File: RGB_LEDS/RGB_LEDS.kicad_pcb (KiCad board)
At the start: 2 copper layers, 21.7 x 28.1 mm, 16 parts, among them IC1 ATTINY202-SSFR, IC2 INA180A4IDBVR, IC3 XC9140A501MR-G, J1 HCZZ0021-2, SW1 SW_Push, U1 MY-2032-08

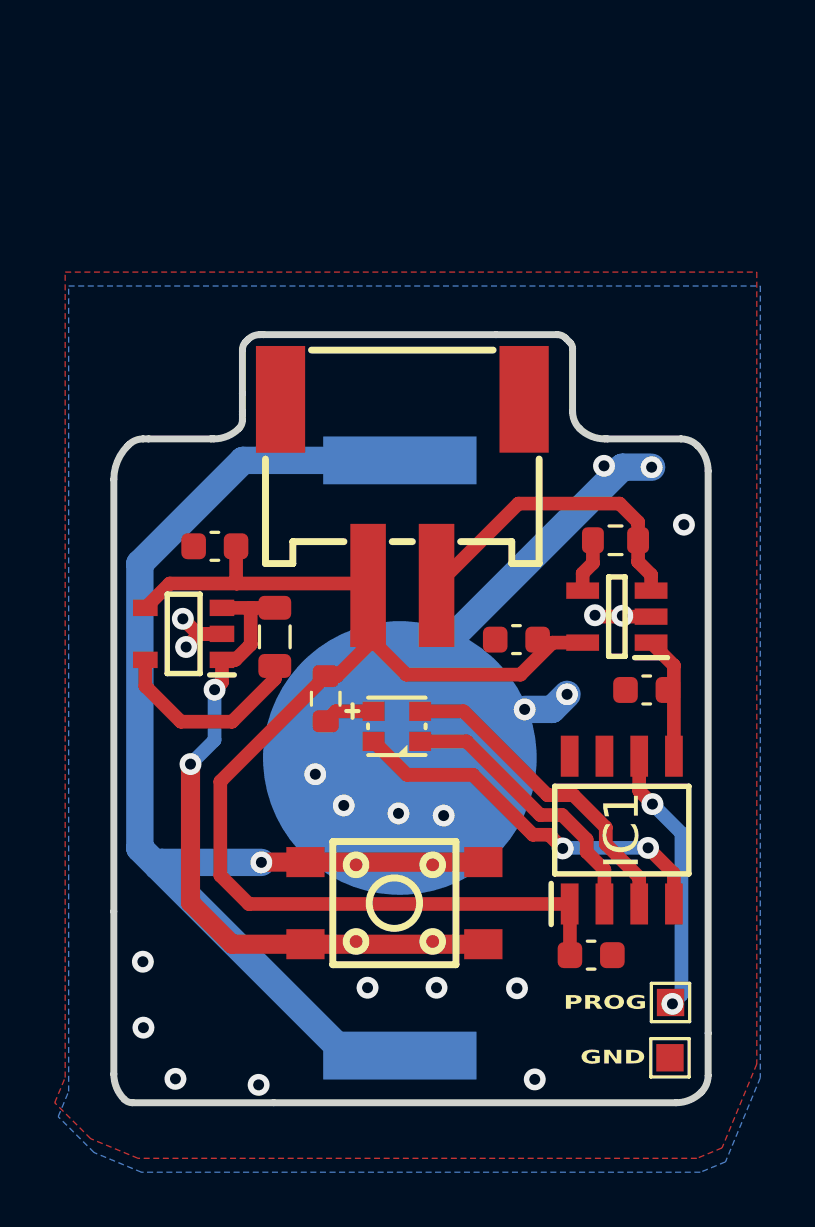
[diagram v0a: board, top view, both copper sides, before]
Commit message: Placa con stm32, selector de voltaje se necesita quitar una vez que se decida por un valor
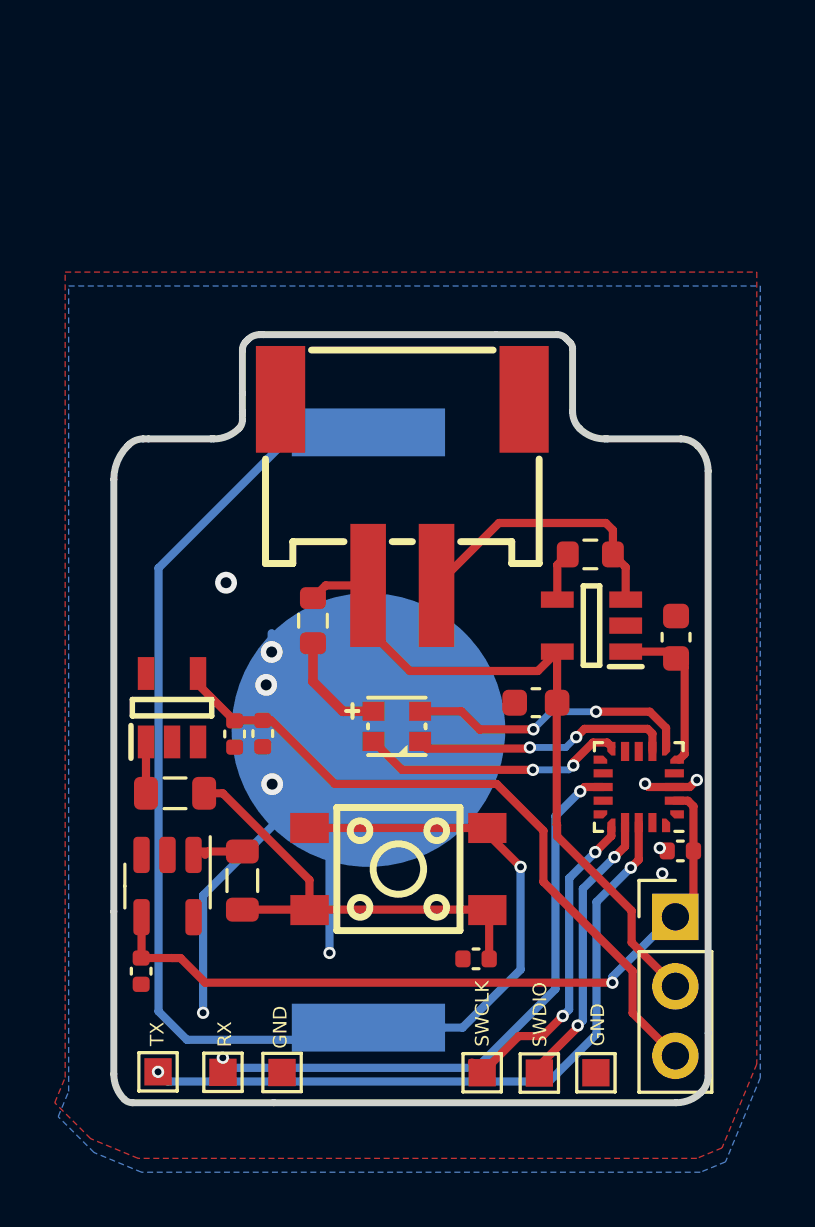
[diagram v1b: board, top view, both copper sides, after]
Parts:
- removed IC3: XC9140A501MR-G, SamacSys_Parts:SOT95P280X130-5N
- added C5: 100n, Capacitor_SMD:C_0402_1005Metric, F.Cu at (158.5, 99.8)
- added C6: 4.7u, Capacitor_SMD:C_0402_1005Metric, F.Cu at (165.9, 95.9)
- added C7: 100n, Capacitor_SMD:C_0402_1005Metric, F.Cu at (150.7, 91.6)
- added J2: Conn_01x03_Pin, Connector_PinHeader_2.54mm:PinHeader_1x03_P2.54mm_Vertical, F.Cu at (165.7, 98.3)
- added L2: 2.2u, Inductor_SMD:L_0805_2012Metric, F.Cu at (147.5, 93.8)
- added U3: STM32C011F4Ux, Package_DFN_QFN:ST_UFQFPN-20_3x3mm_P0.5mm, F.Cu at (164.4, 93.5)
- added U5: TPS613221ADBV, Package_TO_SOT_SMD:SOT-23-5, F.Cu at (147.2, 97.1)
- added U6: ~, TestPoint:TestPoint_Pad_1.0x1.0mm, F.Cu at (146.8, 103.9)
- added U7: ~, TestPoint:TestPoint_Pad_1.0x1.0mm, F.Cu at (160.8, 104.0)
- added U8: ~, TestPoint:TestPoint_Pad_1.0x1.0mm, F.Cu at (158.7, 104.0)
- added U9: ~, TestPoint:TestPoint_Pad_1.0x1.0mm, F.Cu at (162.8, 104.0)
- C2: footprint Capacitor_SMD:C_0603_1608Metric -> Capacitor_SMD:C_0402_1005Metric
- C4: value 100n -> 4.7u; footprint Capacitor_SMD:C_0603_1608Metric -> Capacitor_SMD:C_0402_1005Metric
- IC1: value ATTINY202-SSFR -> TPS613222ADBVR; footprint SamacSys_Parts:SOIC127P600X175-8N -> SamacSys_Parts:SOT95P280X145-5N
- L1: value 4.7u -> 2.2u
- moved IC1 17.0 mm to (147.4, 90.6)
- moved U4 16.3 mm to (149.2, 104.0), turned to 0 degrees
- moved C2 15.8 mm to (146.2, 100.3), turned to 90 degrees
- moved C4 15.3 mm to (149.6, 91.6), turned to -90 degrees
- moved U2 14.4 mm to (151.4, 104.0)
- moved L1 8.98 mm to (149.9, 96.9)
- moved R2 2.89 mm to (152.5, 87.4)
- moved C1 2.41 mm to (160.7, 90.4)
- moved C3 2.21 mm to (165.8, 88.1), turned to 90 degrees
- moved U1 1.54 mm to (154.5, 91.4)
- moved SW1 1.26 mm to (155.6, 96.5)
- moved R1 1.05 mm to (162.6, 85.0)
- moved IC2 0.98 mm to (162.7, 87.6)
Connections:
- C1 pad 1: +5V -> Vused
- C2 pad 2: +5V -> +3.3V
- IC1 pad 1: +5V -> Net-(IC1-SW)
- IC1 pad 2: R -> GND
- IC1 pad 3: G -> unconnected-(IC1-NC_1-Pad3)
- IC1 pad 4: B -> +5V
- IC1 pad 5: REF_OUT -> unconnected-(IC1-NC_2-Pad5)
- IC2 pad 5: +5V -> Vused
- J1 pad 1: +5V -> Vused
- L1 pad 1: Net-(IC3-LX) -> Net-(C5-Pad1)
- L1 pad 2: Net-(IC3-CE) -> Net-(U5-SW)
- R2 pad 2: +5V -> Vused
- SW1 pad 2: Net-(IC3-CE) -> Net-(C5-Pad1)
- U2 pad 1: Net-(IC1-PA0/~{RESET}/UPDI) -> GND
- U4 pad 1: GND -> RX
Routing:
- net +3.3V: track 0.00 -> 27.6 mm, vias 0 -> 1
- net Vused: track 0.00 -> 25.7 mm
- net TX: track 0.00 -> 25.3 mm, vias 0 -> 2
- net Net-(IC3-CE): track 25.2 -> 0.00 mm, vias 2 -> 0
- net +5V: track 48.8 -> 25.5 mm
- net RX: track 0.00 -> 22.0 mm, vias 0 -> 2
- net Net-(C5-Pad1): track 0.00 -> 17.0 mm
- net /SWCLK: track 0.00 -> 12.0 mm, vias 0 -> 2
- net /SWDIO: track 0.00 -> 10.5 mm, vias 0 -> 2
- net Net-(IC1-PA0/~{RESET}/UPDI): track 9.83 -> 0.00 mm, vias 2 -> 0
- net Net-(IC3-LX): track 7.35 -> 0.00 mm
- net Net-(SW1-Pad1): track 46.1 -> 53.2 mm
- net GND: track 26.1 -> 31.2 mm, vias 21 -> 10
- net B: track 14.1 -> 9.66 mm
- net Net-(D1-Pad3): track 1.90 -> 4.06 mm
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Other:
- board text added: "RX"
- board text added: "SWCLK"
- board text added: "SWDIO"
- board text added: "TX"
- board text removed: "PROG"

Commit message: final version, longer connector, 3.3 only
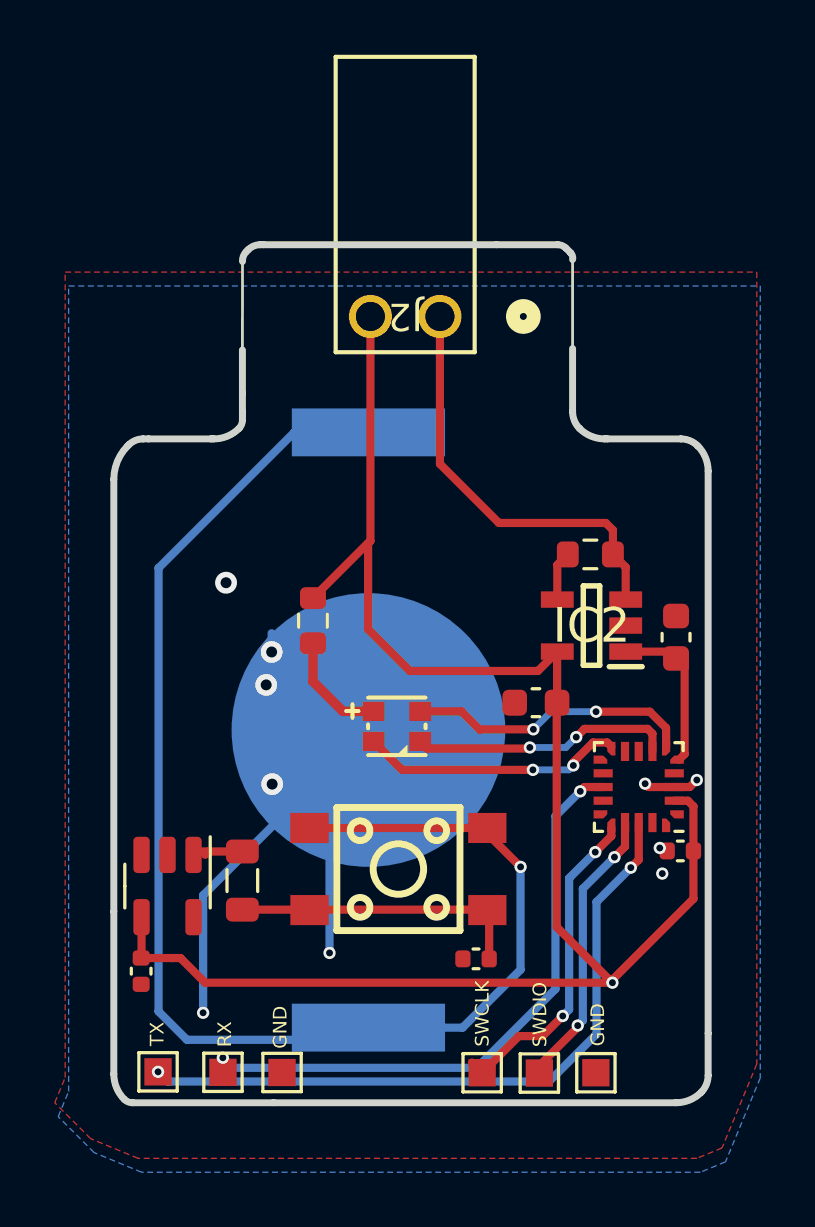
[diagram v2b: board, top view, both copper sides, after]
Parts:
- removed C4: 4.7u, Capacitor_SMD:C_0402_1005Metric
- removed C7: 100n, Capacitor_SMD:C_0402_1005Metric
- removed IC1: TPS613222ADBVR, SamacSys_Parts:SOT95P280X145-5N
- removed J1: HCZZ0021-2, Library:CONN-SMD_2P-P2.50-A2501-WF-02A
- removed L2: 2.2u, Inductor_SMD:L_0805_2012Metric
- IC2: footprint SamacSys_Parts:SOT95P280X145-5N -> SamacSys:SOT95P280X145-5N
- J2: value Conn_01x03_Pin -> 22122021; footprint Connector_PinHeader_2.54mm:PinHeader_1x03_P2.54mm_Vertical -> 0022122021:CONN_A-4094-02A_MOL
- U3: value STM32C011F4Ux -> STM32C011F6U6TR
- moved J2 23.6 mm to (157.1, 76.3), turned to 180 degrees
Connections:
- C1 pad 1: Vused -> +3.3V
- IC2 pad 5: Vused -> +3.3V
- J2 pad 1: +3.3V -> REF
- J2 pad 2: Vused -> +3.3V
- R2 pad 2: Vused -> +3.3V
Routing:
- net +3.3V: track 27.6 -> 62.6 mm
- net Vused: track 25.7 -> 0.00 mm
- net +5V: track 25.5 -> 0.00 mm
- net Net-(C5-Pad1): track 17.0 -> 10.8 mm
- net REF: track 10.2 -> 15.4 mm
- net Net-(IC1-SW): track 1.88 -> 0.00 mm
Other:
- board size 21.7 x 28.1 mm -> 21.7 x 31.4 mm

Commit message: Added selector
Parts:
- added S1: CL-SB-23B-01T, SamacSys_Parts:CLSB23B01T, F.Cu at (148.6, 87.5)
- SW1: value SW_Push -> TSC015A05026A
- moved R2 1.07 mm to (153.3, 88.1)
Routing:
- net Net-(D1-Pad3): track 4.06 -> 3.04 mm
- net GND: vias 10 -> 11
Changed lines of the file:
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@@
   (net 26 "unconnected-(U5-NC-Pad5)")
   (net 27 "Net-(SW1-Pad1)")
+  (net 28 "unconnected-(S1-NO_1-Pad1)")
+  (net 29 "unconnected-(S1-NC_1-Pad2)")
+  (net 30 "unconnected-(S1-COM_1-Pad3)")
+  (net 31 "unconnected-(S1-NO_2-Pad4)")
+  (net 32 "unconnected-(S1-NO_3-Pad5)")
+  (net 33 "unconnected-(S1-NC_2-Pad6)")
+  (net 34 "unconnected-(S1-COM_2-Pad7)")
+  (net 35 "unconnected-(S1-NO_4-Pad8)")
   (footprint "Resistor_SMD:R_0603_1608Metric" (layer "F.Cu")
     (at 162.641 85.027)
@@
         (effects (font (size 1.143 1.143) (thickness 0.1524)) (justify left))
     )
-    (fp_text value "SW_Push" (at 0 -5.116322) (layer "F.Fab") hide
+    (fp_text value "TSC015A05026A" (at 0 -5.116322) (layer "F.Fab") hide
         (effects (font (size 1.143 1.143) (thickness 0.1524)) (justify left))
     )
@@
   )
   (footprint "Resistor_SMD:R_0603_1608Metric" (layer "F.Cu")
-    (at 152.505 87.448 90)
+    (at 153.319 88.138 90)
     (descr "Resistor SMD 0603 (1608 Metric), square (rectangular) end terminal, IPC_7351 nominal, (Body size source: IPC-SM-782 page 72, https://www.pcb-3d.com/wordpress/wp-content/uploads/ipc-sm-782a_amendment_1_and_2.pdf), generated with kicad-footprint-generator")
     (tags "resistor")
@@
     (pad "1" smd rect (at 0 0) (size 1 1) (layers "F.Cu" "F.Mask")
       (net 21 "/SWDIO") (pinfunction "PAD") (pintype "input"))
+  )
+  (footprint "SamacSys_Parts:CLSB23B01T" (layer "F.Cu")
+    (at 148.634 87.451 90)
+    (descr "CL-SB-23B-01T-1")
+    (tags "Switch")
+    (property "Arrow Part Number" "")
+    (property "Arrow Price/Stock" "")
+    (property "Height" "3.5")
+    (property "Manufacturer_Name" "Nidec Copal")
+    (property "Manufacturer_Part_Number" "CL-SB-23B-01T")
+    (property "Mouser Part Number" "229-CL-SB-23B-01T")
+    (property "Mouser Price/Stock" "https://www.mouser.co.uk/ProductDetail/Nidec-Components/CL-SB-23B-01T?qs=XeJtXLiO41QX0zcc2Dzzgg%3D%3D")
+    (property "Sheetfile" "RGB_LEDS.kicad_sch")
+    (property "Sheetname" "")
+    (property "ki_description" "SLIDE SWITCH, DP3T, 0.2A, 12VDC, SMD; Contact Configuration:DP3T; Switch Operation:-; Switch Mounting:SMD; Product Range:CL-SB Series; Contact Current Max:200mA; Contact Voltage AC Max:-; Contact Voltage DC Max:12V; RoHS Compliant: Yes")
+    (attr smd)
+    (fp_text reference "S1" (at 0 0 90) (layer "F.SilkS")
+        (effects (font (size 1.27 1.27) (thickness 0.254)))
+    )
+    (fp_text value "CL-SB-23B-01T" (at 0 0 90) (layer "F.SilkS") hide
+        (effects (font (size 1.27 1.27) (thickness 0.254)))
+    )
+    (fp_text user "${REFERENCE}" (at 0 0 90) (layer "F.Fab")
+        (effects (font (size 1.27 1.27) (thickness 0.254)))
+    )
+    (fp_line (start -6 -1.75) (end -6 1.75)
+      (stroke (width 0.1) (type solid)) (layer "F.SilkS"))
+    (fp_line (start -6 1.75) (end -5 1.75)
+      (stroke (width 0.1) (type solid)) (layer "F.SilkS"))
+    (fp_line (start -5 -1.75) (end -6 -1.75)
+      (stroke (width 0.1) (type solid)) (layer "F.SilkS"))
+    (fp_line (start -1 -1.75) (end 1 -1.75)
+      (stroke (width 0.1) (type solid)) (layer "F.SilkS"))
+    (fp_line (start -1 1.75) (end 1 1.75)
+      (stroke (width 0.1) (type solid)) (layer "F.SilkS"))
+    (fp_line (start 5 -1.75) (end 6 -1.75)
+      (stroke (width 0.1) (type solid)) (layer "F.SilkS"))
+    (fp_line (start 6 -1.75) (end 6 1.75)
+      (stroke (width 0.1) (type solid)) (layer "F.SilkS"))
+    (fp_line (start 6 1.75) (end 5 1.75)
+      (stroke (width 0.1) (type solid)) (layer "F.SilkS"))
+    (fp_line (start -7 -3.9) (end 7 -3.9)
+      (stroke (width 0.1) (type solid)) (layer "F.CrtYd"))
+    (fp_line (start -7 3.9) (end -7 -3.9)
+      (stroke (width 0.1) (type solid)) (layer "F.CrtYd"))
+    (fp_line (start 7 -3.9) (end 7 3.9)
+      (stroke (width 0.1) (type solid)) (layer "F.CrtYd"))
+    (fp_line (start 7 3.9) (end -7 3.9)
+      (stroke (width 0.1) (type solid)) (layer "F.CrtYd"))
+    (fp_line (start -6 -1.75) (end 6 -1.75)
+      (stroke (width 0.2) (type solid)) (layer "F.Fab"))
+    (fp_line (start -6 1.75) (end -6 -1.75)
+      (stroke (width 0.2) (type solid)) (layer "F.Fab"))
+    (fp_line (start 6 -1.75) (end 6 1.75)
+      (stroke (width 0.2) (type solid)) (layer "F.Fab"))
+    (fp_line (start 6 1.75) (end -6 1.75)
+      (stroke (width 0.2) (type solid)) (layer "F.Fab"))
+    (pad "1" smd rect (at -4 2.2 90) (size 1.2 1.4) (layers "F.Cu" "F.Paste" "F.Mask")
+      (net 28 "unconnected-(S1-NO_1-Pad1)") (pinfunction "NO_1") (pintype "passive"))
+    (pad "2" smd rect (at -2 2.2 90) (size 1.2 1.4) (layers "F.Cu" "F.Paste" "F.Mask")
+      (net 29 "unconnected-(S1-NC_1-Pad2)") (pinfunction "NC_1") (pintype "passive"))
+    (pad "3" smd rect (at 2 2.2 90) (size 1.2 1.4) (layers "F.Cu" "F.Paste" "F.Mask")
+      (net 30 "unconnected-(S1-COM_1-Pad3)") (pinfunction "COM_1") (pintype "passive"))
+    (pad "4" smd rect (at 4 2.2 90) (size 1.2 1.4) (layers "F.Cu" "F.Paste" "F.Mask")
+      (net 31 "unconnected-(S1-NO_2-Pad4)") (pinfunction "NO_2") (pintype "passive"))
+    (pad "5" smd rect (at -4 -2.2 90) (size 1.2 1.4) (layers "F.Cu" "F.Paste" "F.Mask")
+      (net 32 "unconnected-(S1-NO_3-Pad5)") (pinfunction "NO_3") (pintype "passive"))
+    (pad "6" smd rect (at -2 -2.2 90) (size 1.2 1.4) (layers "F.Cu" "F.Paste" "F.Mask")
+      (net 33 "unconnected-(S1-NC_2-Pad6)") (pinfunction "NC_2") (pintype "passive"))
+    (pad "7" smd rect (at 2 -2.2 90) (size 1.2 1.4) (layers "F.Cu" "F.Paste" "F.Mask")
+      (net 34 "unconnected-(S1-COM_2-Pad7)") (pinfunction "COM_2") (pintype "passive"))
+    (pad "8" smd rect (at 4 -2.2 90) (size 1.2 1.4) (layers "F.Cu" "F.Paste" "F.Mask")
+      (net 35 "unconnected-(S1-NO_4-Pad8)") (pinfunction "NO_4") (pintype "passive"))
+    (model "D:\\ProgramFiles\\KiCad\\7.0\\Components\\SamacSys_Parts.3dshapes\\CL-SB-23B-01T.stp"
+      (offset (xyz 0 0 0))
+      (scale (xyz 1 1 1))
+      (rotate (xyz 0 0 0))
+    )
   )
   (footprint "Package_DFN_QFN:ST_UFQFPN-20_3x3mm_P0.5mm" (layer "F.Cu")
@@
   (via (at 165.269 96.689) (size 0.45) (drill 0.25) (layers "F.Cu" "B.Cu") (net 1))
   (via (at 166.532 93.27) (size 0.45) (drill 0.25) (layers "F.Cu" "B.Cu") (net 1))
+  (via (at 158.736 90.226) (size 0.8) (drill 0.4) (layers "F.Cu" "B.Cu") (net 1))
   (via (at 153.11 99.589) (size 0.45) (drill 0.25) (layers "F.Cu" "B.Cu") (net 1))
   (via (at 151.014 93.421) (size 0.8) (drill 0.4) (layers "F.Cu" "B.Cu") (net 1))
@@
   (segment (start 160.558 91.419) (end 161.203 90.774) (width 0.25) (layer "B.Cu") (net 6))
   (segment (start 161.203 90.774) (end 162.849 90.774) (width 0.25) (layer "B.Cu") (net 6))
+  (segment (start 153.319 85.824826) (end 153.319 87.313) (width 0.3) (layer "F.Cu") (net 7))
   (segment (start 154.60472 84.539106) (end 154.60472 76.33208) (width 0.3) (layer "F.Cu") (net 7))
   (segment (start 166.409 94.231024) (end 166.409 97.609) (width 0.3) (layer "F.Cu") (net 7))
@@
   (segment (start 147.354 99.775) (end 147.355 99.776) (width 0.3) (layer "F.Cu") (net 7))
   (segment (start 160.725 89.286) (end 156.046025 89.286) (width 0.3) (layer "F.Cu") (net 7))
+  (segment (start 154.520066 84.62376) (end 153.319 85.824826) (width 0.3) (layer "F.Cu") (net 7))
   (segment (start 166.203976 94.026) (end 166.409 94.231024) (width 0.3) (layer "F.Cu") (net 7))
   (segment (start 154.520066 87.760041) (end 154.520066 84.62376) (width 0.3) (layer "F.Cu") (net 7))
@@
   (segment (start 161.412 98.6405) (end 161.412 90.459) (width 0.3) (layer "F.Cu") (net 7))
   (segment (start 161.433 88.578) (end 160.725 89.286) (width 0.3) (layer "F.Cu") (net 7))
-  (segment (start 154.50424 84.62376) (end 152.505 86.623) (width 0.3) (layer "F.Cu") (net 7))
   (segment (start 165.709 94.026) (end 166.203976 94.026) (width 0.3) (layer "F.Cu") (net 7))
   (segment (start 163.4475 100.5705) (end 163.4475 100.676) (width 0.3) (layer "F.Cu") (net 7))
@@
   (segment (start 161.426 88.585) (end 161.433 88.578) (width 0.3) (layer "F.Cu") (net 7))
   (segment (start 146.241 98.2825) (end 146.241 99.761) (width 0.3) (layer "F.Cu") (net 7))
-  (segment (start 154.520066 84.62376) (end 154.50424 84.62376) (width 0.3) (layer "F.Cu") (net 7))
   (segment (start 147.355 99.776) (end 147.664999 99.776) (width 0.3) (layer "F.Cu") (net 7))
   (via (at 163.4475 100.676) (size 0.45) (drill 0.25) (layers "F.Cu" "B.Cu") (net 7))
   (segment (start 153.59409 90.76009) (end 154.719862 90.76009) (width 0.35) (layer "F.Cu") (net 8))
-  (segment (start 152.505 89.671) (end 153.59409 90.76009) (width 0.35) (layer "F.Cu") (net 8))
-  (segment (start 152.505 88.273) (end 152.505 89.671) (width 0.35) (layer "F.Cu") (net 8))
+  (segment (start 153.319 88.963) (end 153.319 90.485) (width 0.35) (layer "F.Cu") (net 8))
+  (segment (start 153.319 90.485) (end 153.59409 90.76009) (width 0.35) (layer "F.Cu") (net 8))
   (segment (start 158.944 98.090194) (end 158.87693 98.023124) (width 0.3) (layer "F.Cu") (net 9))
   (segment (start 149.925 98.0075) (end 149.927 98.0055) (width 0.3) (layer "F.Cu") (net 9))
